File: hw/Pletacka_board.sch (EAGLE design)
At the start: 55 parts, among them U1 LM75BDP-NEW, U2 EL357N(A)(TA)-G, U3 EL357N(A)(TA)-G, U4 EL357N(A)(TA)-G, U5 EL357N(A)(TA)-G, U6 TPS54231D

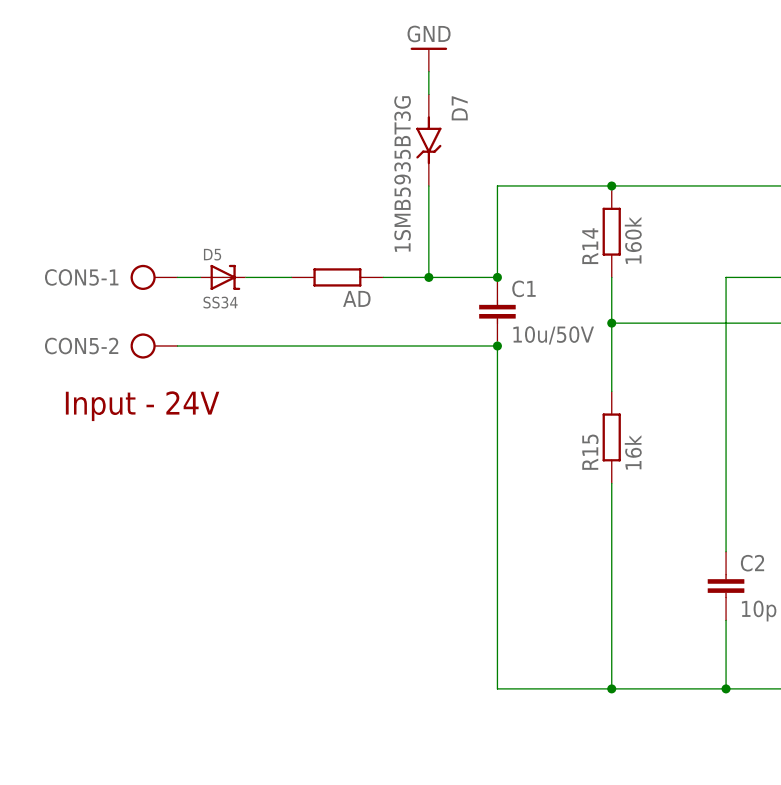
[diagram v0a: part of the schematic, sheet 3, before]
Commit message: Improve schema for step-down input
- improve readability of over-voltage protection in schema
- fix some minor issues (LCSC_IDs, ...)
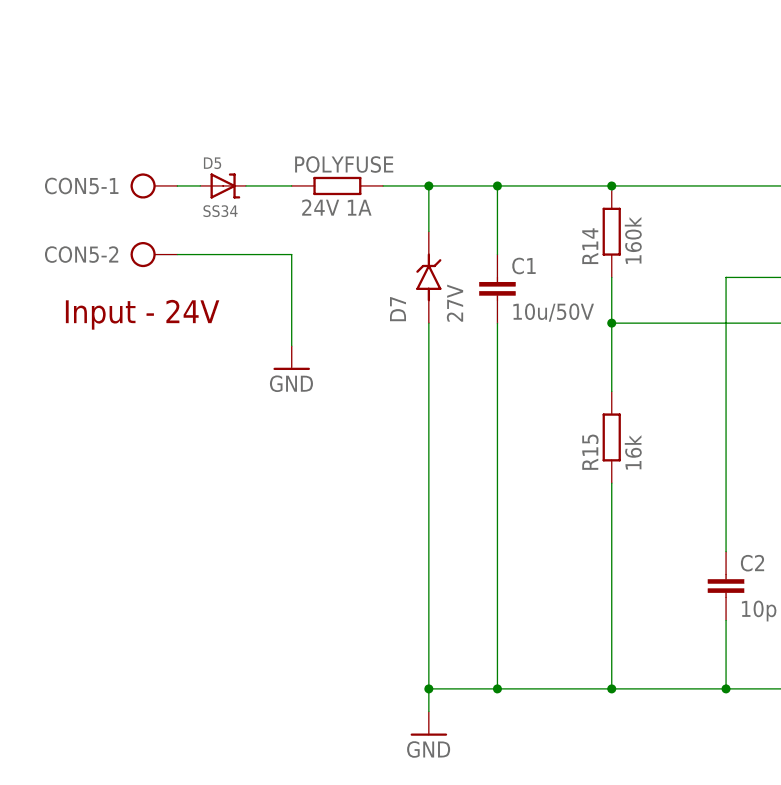
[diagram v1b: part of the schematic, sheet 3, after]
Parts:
- removed AD: (no value), rcl_upravena:R-EU_R1206
- added POLYFUSE: 24V 1A, rcl_upravena:R-EU_R1206
- D7: value 1SMB5935BT3G -> 27V; LCSC_ID (none) -> C49827
- U6: DESCRIPTION (none) -> 3.5 to 28V Input, 2A, 570kHz Step-Down Converter with Eco-m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
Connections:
- net N$4: now also POLYFUSE.2; no longer AD.2
- net VIN: now also POLYFUSE.1; no longer AD.1
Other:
- moved on the sheet: C1, CON5-1, CON5-2, D5, D7

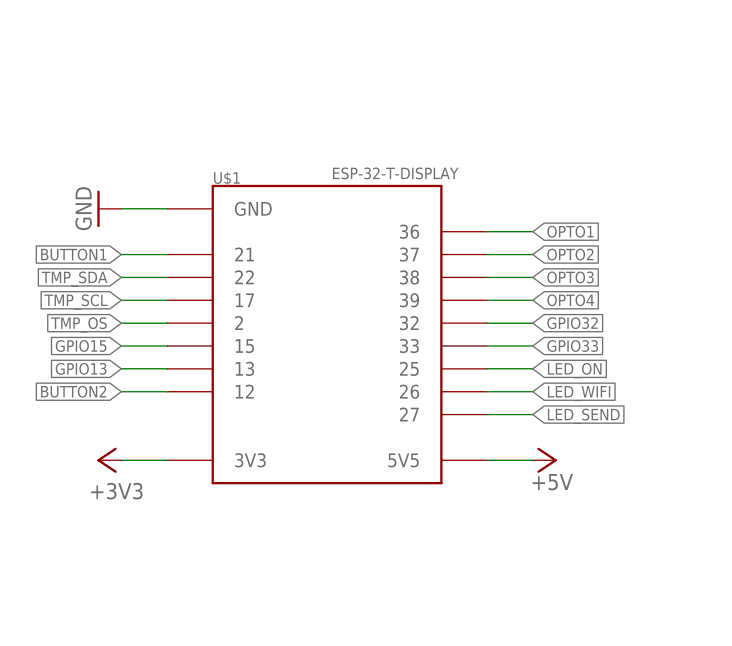
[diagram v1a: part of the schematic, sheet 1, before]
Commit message: Fix Beware of tombstoning (close #9)
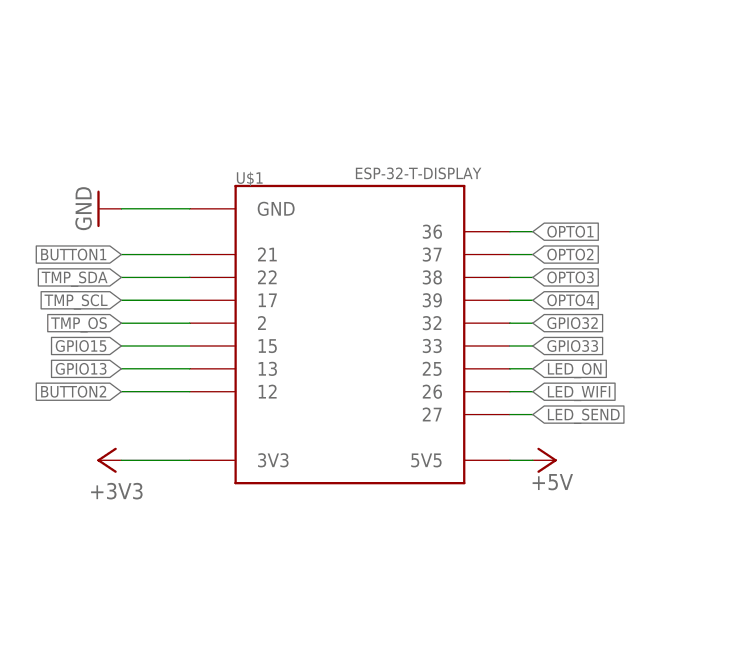
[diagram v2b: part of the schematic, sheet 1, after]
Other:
- moved on the sheet: U$1
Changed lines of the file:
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@@
 </spice>
 <attribute name="LCSC_ID" value="C22813"/>
-<attribute name="MFR_ID" value="nSMD050-24V
-"/>
+<attribute name="MFR_ID" value="nSMD050-24V "/>
 </part>
 <part name="GND14" library="supply1" library_urn="urn:adsk.eagle:library:371" deviceset="GND" device=""/>
@@
 <attribute name="SHEET" x="230.505" y="5.08" size="2.54" layer="94"/>
 </instance>
-<instance part="U$1" gate="G$1" x="66.04" y="96.52" smashed="yes">
-<attribute name="NAME" x="53.34" y="114.554" size="1.27" layer="95" font="vector" ratio="20"/>
-<attribute name="VALUE" x="66.548" y="115.062" size="1.27" layer="96" font="vector" ratio="20"/>
+<instance part="U$1" gate="G$1" x="68.58" y="96.52" smashed="yes">
+<attribute name="NAME" x="55.88" y="114.554" size="1.27" layer="95" font="vector" ratio="20"/>
+<attribute name="VALUE" x="69.088" y="115.062" size="1.27" layer="96" font="vector" ratio="20"/>
 </instance>
 <instance part="GND1" gate="1" x="40.64" y="111.76" smashed="yes" rot="R270">
@@
 <pinref part="GND1" gate="1" pin="GND"/>
 <pinref part="U$1" gate="G$1" pin="GND"/>
-<wire x1="43.18" y1="111.76" x2="48.26" y2="111.76" width="0.1524" layer="91"/>
+<wire x1="43.18" y1="111.76" x2="50.8" y2="111.76" width="0.1524" layer="91"/>
 </segment>
 <segment>
@@
 <pinref part="+3V1" gate="G$1" pin="+3V3"/>
 <pinref part="U$1" gate="G$1" pin="3V3"/>
-<wire x1="43.18" y1="83.82" x2="48.26" y2="83.82" width="0.1524" layer="91"/>
+<wire x1="43.18" y1="83.82" x2="50.8" y2="83.82" width="0.1524" layer="91"/>
 </segment>
 <segment>
@@
 <pinref part="U$1" gate="G$1" pin="5V5"/>
 <pinref part="P+1" gate="1" pin="+5V"/>
-<wire x1="83.82" y1="83.82" x2="88.9" y2="83.82" width="0.1524" layer="91"/>
+<wire x1="86.36" y1="83.82" x2="88.9" y2="83.82" width="0.1524" layer="91"/>
 </segment>
 <segment>
@@
 <segment>
 <pinref part="U$1" gate="G$1" pin="39"/>
-<wire x1="83.82" y1="101.6" x2="88.9" y2="101.6" width="0.1524" layer="91"/>
+<wire x1="86.36" y1="101.6" x2="88.9" y2="101.6" width="0.1524" layer="91"/>
 <label x="88.9" y="101.6" size="1.27" layer="95" xref="yes"/>
 </segment>
@@
 <segment>
 <pinref part="U$1" gate="G$1" pin="38"/>
-<wire x1="83.82" y1="104.14" x2="88.9" y2="104.14" width="0.1524" layer="91"/>
+<wire x1="86.36" y1="104.14" x2="88.9" y2="104.14" width="0.1524" layer="91"/>
 <label x="88.9" y="104.14" size="1.27" layer="95" xref="yes"/>
 </segment>
@@
 <segment>
 <pinref part="U$1" gate="G$1" pin="37"/>
-<wire x1="83.82" y1="106.68" x2="88.9" y2="106.68" width="0.1524" layer="91"/>
+<wire x1="86.36" y1="106.68" x2="88.9" y2="106.68" width="0.1524" layer="91"/>
 <label x="88.9" y="106.68" size="1.27" layer="95" xref="yes"/>
 </segment>
@@
 <segment>
 <pinref part="U$1" gate="G$1" pin="36"/>
-<wire x1="83.82" y1="109.22" x2="88.9" y2="109.22" width="0.1524" layer="91"/>
+<wire x1="86.36" y1="109.22" x2="88.9" y2="109.22" width="0.1524" layer="91"/>
 <label x="88.9" y="109.22" size="1.27" layer="95" xref="yes"/>
 </segment>
@@
 <segment>
 <pinref part="U$1" gate="G$1" pin="26"/>
-<wire x1="83.82" y1="91.44" x2="88.9" y2="91.44" width="0.1524" layer="91"/>
+<wire x1="86.36" y1="91.44" x2="88.9" y2="91.44" width="0.1524" layer="91"/>
 <label x="88.9" y="91.44" size="1.27" layer="95" xref="yes"/>
 </segment>
@@
 <segment>
 <pinref part="U$1" gate="G$1" pin="27"/>
-<wire x1="83.82" y1="88.9" x2="88.9" y2="88.9" width="0.1524" layer="91"/>
+<wire x1="86.36" y1="88.9" x2="88.9" y2="88.9" width="0.1524" layer="91"/>
 <label x="88.9" y="88.9" size="1.27" layer="95" xref="yes"/>
 </segment>
@@
 <segment>
 <pinref part="U$1" gate="G$1" pin="21"/>
-<wire x1="48.26" y1="106.68" x2="43.18" y2="106.68" width="0.1524" layer="91"/>
+<wire x1="50.8" y1="106.68" x2="43.18" y2="106.68" width="0.1524" layer="91"/>
 <label x="43.18" y="106.68" size="1.27" layer="95" rot="R180" xref="yes"/>
 </segment>
@@
 <segment>
 <pinref part="U$1" gate="G$1" pin="12"/>
-<wire x1="48.26" y1="91.44" x2="43.18" y2="91.44" width="0.1524" layer="91"/>
+<wire x1="50.8" y1="91.44" x2="43.18" y2="91.44" width="0.1524" layer="91"/>
 <label x="43.18" y="91.44" size="1.27" layer="95" rot="R180" xref="yes"/>
 </segment>
@@
 <segment>
 <pinref part="U$1" gate="G$1" pin="22"/>
-<wire x1="48.26" y1="104.14" x2="43.18" y2="104.14" width="0.1524" layer="91"/>
+<wire x1="50.8" y1="104.14" x2="43.18" y2="104.14" width="0.1524" layer="91"/>
 <label x="43.18" y="104.14" size="1.27" layer="95" rot="R180" xref="yes"/>
 </segment>
@@
 <segment>
 <pinref part="U$1" gate="G$1" pin="17"/>
-<wire x1="48.26" y1="101.6" x2="43.18" y2="101.6" width="0.1524" layer="91"/>
+<wire x1="50.8" y1="101.6" x2="43.18" y2="101.6" width="0.1524" layer="91"/>
 <label x="43.18" y="101.6" size="1.27" layer="95" rot="R180" xref="yes"/>
 </segment>
@@
 <segment>
 <pinref part="U$1" gate="G$1" pin="2"/>
-<wire x1="48.26" y1="99.06" x2="43.18" y2="99.06" width="0.1524" layer="91"/>
+<wire x1="50.8" y1="99.06" x2="43.18" y2="99.06" width="0.1524" layer="91"/>
 <label x="43.18" y="99.06" size="1.27" layer="95" rot="R180" xref="yes"/>
 </segment>
@@
 <segment>
 <pinref part="U$1" gate="G$1" pin="15"/>
-<wire x1="48.26" y1="96.52" x2="43.18" y2="96.52" width="0.1524" layer="91"/>
+<wire x1="50.8" y1="96.52" x2="43.18" y2="96.52" width="0.1524" layer="91"/>
 <label x="43.18" y="96.52" size="1.27" layer="95" rot="R180" xref="yes"/>
 </segment>
@@
 <segment>
 <pinref part="U$1" gate="G$1" pin="13"/>
-<wire x1="48.26" y1="93.98" x2="43.18" y2="93.98" width="0.1524" layer="91"/>
+<wire x1="50.8" y1="93.98" x2="43.18" y2="93.98" width="0.1524" layer="91"/>
 <label x="43.18" y="93.98" size="1.27" layer="95" rot="R180" xref="yes"/>
 </segment>
@@
 <segment>
 <pinref part="U$1" gate="G$1" pin="32"/>
-<wire x1="83.82" y1="99.06" x2="88.9" y2="99.06" width="0.1524" layer="91"/>
+<wire x1="86.36" y1="99.06" x2="88.9" y2="99.06" width="0.1524" layer="91"/>
 <label x="88.9" y="99.06" size="1.27" layer="95" xref="yes"/>
 </segment>
@@
 <segment>
 <pinref part="U$1" gate="G$1" pin="33"/>
-<wire x1="83.82" y1="96.52" x2="88.9" y2="96.52" width="0.1524" layer="91"/>
+<wire x1="86.36" y1="96.52" x2="88.9" y2="96.52" width="0.1524" layer="91"/>
 <label x="88.9" y="96.52" size="1.27" layer="95" xref="yes"/>
 </segment>
@@
 <segment>
 <pinref part="U$1" gate="G$1" pin="25"/>
-<wire x1="83.82" y1="93.98" x2="88.9" y2="93.98" width="0.1524" layer="91"/>
+<wire x1="86.36" y1="93.98" x2="88.9" y2="93.98" width="0.1524" layer="91"/>
 <label x="88.9" y="93.98" size="1.27" layer="95" xref="yes"/>
 </segment>

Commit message: Add pull-up resistors on I2C (close #14)
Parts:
- added R17, R18: 4k7, rcl_upravena:R-EU_R0603
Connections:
- net +3V3: now also R17.2, R18.2
- net TMP_SCL: now also R17.1
- net TMP_SDA: now also R18.1
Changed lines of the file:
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@@
 </part>
 <part name="GND15" library="supply1" library_urn="urn:adsk.eagle:library:371" deviceset="GND" device=""/>
+<part name="R17" library="rcl_upravena" deviceset="R-EU_" device="R0603" value="4k7">
+<attribute name="LCSC_ID" value="C23162"/>
+</part>
+<part name="R18" library="rcl_upravena" deviceset="R-EU_" device="R0603" value="4k7">
+<attribute name="LCSC_ID" value="C23162"/>
+</part>
+<part name="+3V8" library="supply1" library_urn="urn:adsk.eagle:library:371" deviceset="+3V3" device=""/>
+<part name="+3V9" library="supply1" library_urn="urn:adsk.eagle:library:371" deviceset="+3V3" device=""/>
 </parts>
 <sheets>
@@
 <attribute name="LCSC_ID" x="43.18" y="22.86" size="1.778" layer="96" rot="R90" display="off"/>
 </instance>
+<instance part="R17" gate="G$1" x="157.48" y="73.66" smashed="yes" rot="R90">
+<attribute name="NAME" x="155.9814" y="69.85" size="1.778" layer="95" rot="R90"/>
+<attribute name="VALUE" x="160.782" y="69.85" size="1.778" layer="96" rot="R90"/>
+<attribute name="LCSC_ID" x="157.48" y="73.66" size="1.778" layer="96" rot="R90" display="off"/>
+</instance>
+<instance part="R18" gate="G$1" x="220.98" y="81.28" smashed="yes" rot="R90">
+<attribute name="NAME" x="219.4814" y="77.47" size="1.778" layer="95" rot="R90"/>
+<attribute name="VALUE" x="224.282" y="77.47" size="1.778" layer="96" rot="R90"/>
+<attribute name="LCSC_ID" x="220.98" y="81.28" size="1.778" layer="96" rot="R90" display="off"/>
+</instance>
+<instance part="+3V8" gate="G$1" x="157.48" y="83.82" smashed="yes">
+<attribute name="VALUE" x="160.02" y="86.36" size="1.778" layer="96" rot="R180"/>
+</instance>
+<instance part="+3V9" gate="G$1" x="220.98" y="91.44" smashed="yes">
+<attribute name="VALUE" x="223.52" y="93.98" size="1.778" layer="96" rot="R180"/>
+</instance>
 </instances>
 <busses>
@@
 <pinref part="U1" gate="G$1" pin="SDA"/>
 <wire x1="215.9" y1="73.66" x2="220.98" y2="73.66" width="0.1524" layer="91"/>
-<label x="220.98" y="73.66" size="1.27" layer="95" xref="yes"/>
+<label x="228.6" y="73.66" size="1.27" layer="95" xref="yes"/>
+<pinref part="R18" gate="G$1" pin="1"/>
+<wire x1="220.98" y1="73.66" x2="228.6" y2="73.66" width="0.1524" layer="91"/>
+<wire x1="220.98" y1="76.2" x2="220.98" y2="73.66" width="0.1524" layer="91"/>
+<junction x="220.98" y="73.66"/>
 </segment>
 </net>
 <net name="TMP_SCL" class="0">
 <segment>
+<label x="147.32" y="68.58" size="1.27" layer="95" rot="R180" xref="yes"/>
+<pinref part="R17" gate="G$1" pin="1"/>
+<wire x1="157.48" y1="68.58" x2="147.32" y2="68.58" width="0.1524" layer="91"/>
 <pinref part="U1" gate="G$1" pin="SCL"/>
-<wire x1="180.34" y1="68.58" x2="175.26" y2="68.58" width="0.1524" layer="91"/>
-<label x="175.26" y="68.58" size="1.27" layer="95" rot="R180" xref="yes"/>
+<wire x1="157.48" y1="68.58" x2="180.34" y2="68.58" width="0.1524" layer="91"/>
+<junction x="157.48" y="68.58"/>
 </segment>
 </net>
@@
 <pinref part="R13" gate="G$1" pin="2"/>
 <pinref part="+3V6" gate="G$1" pin="+3V3"/>
+</segment>
+<segment>
+<pinref part="+3V8" gate="G$1" pin="+3V3"/>
+<pinref part="R17" gate="G$1" pin="2"/>
+<wire x1="157.48" y1="81.28" x2="157.48" y2="78.74" width="0.1524" layer="91"/>
+</segment>
+<segment>
+<pinref part="+3V9" gate="G$1" pin="+3V3"/>
+<pinref part="R18" gate="G$1" pin="2"/>
+<wire x1="220.98" y1="88.9" x2="220.98" y2="86.36" width="0.1524" layer="91"/>
 </segment>
 </net>
@@
 <segment>
 <pinref part="U1" gate="G$1" pin="OS"/>
-<wire x1="215.9" y1="71.12" x2="220.98" y2="71.12" width="0.1524" layer="91"/>
-<label x="220.98" y="71.12" size="1.27" layer="95" xref="yes"/>
-</segment>
-</net>
+<wire x1="215.9" y1="71.12" x2="228.6" y2="71.12" width="0.1524" layer="91"/>
+<label x="228.6" y="71.12" size="1.27" layer="95" xref="yes"/>
+</segment>
+</net>

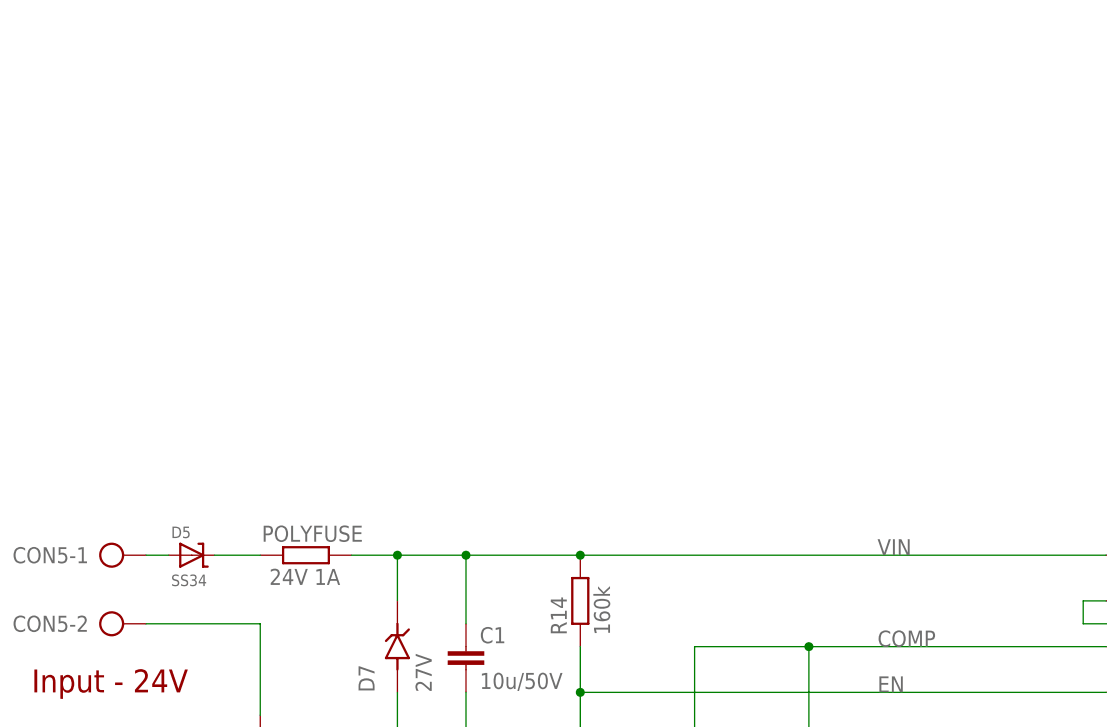
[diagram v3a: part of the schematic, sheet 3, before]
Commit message: Add input power voltage mesurement
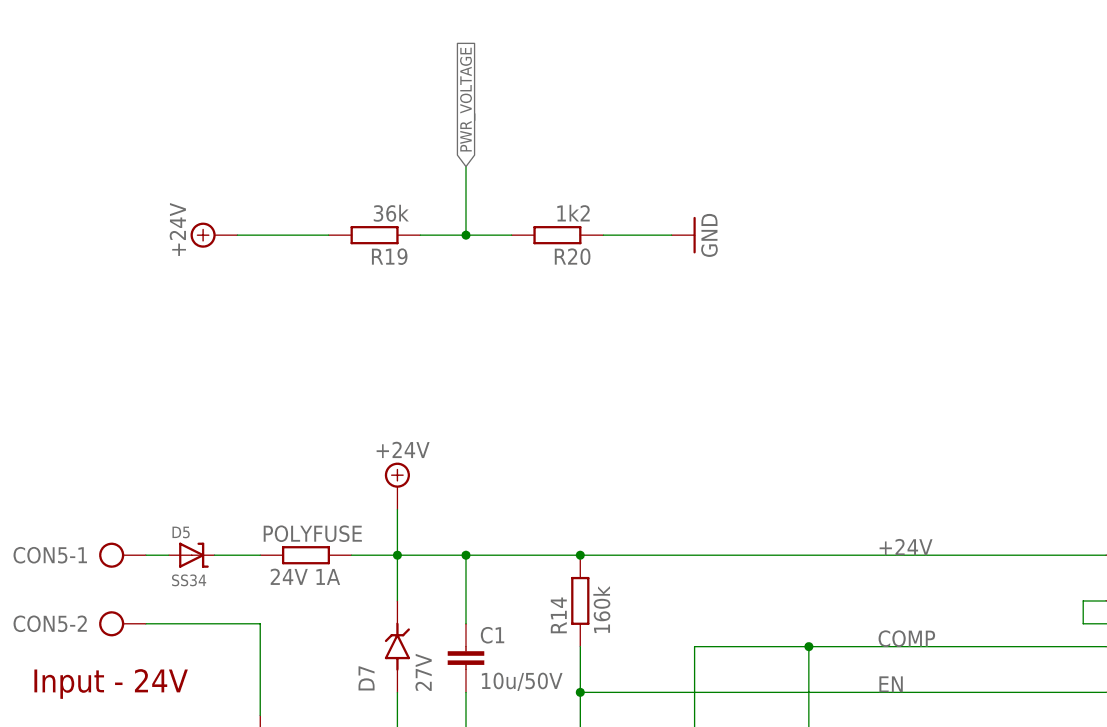
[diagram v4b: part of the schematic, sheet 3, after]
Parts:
- removed JP2, JP3: (no value), pinhead:PINHD-1X4
- added JP4, JP5: (no value), pinhead:PINHD-1X3
- added R19: 36k, rcl_upravena:R-EU_R0603
- added R20: 1k2, rcl_upravena:R-EU_R0603
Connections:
- removed net GPIO32: JP2.1, U$1.32
- removed net VIN: C1.1, D7.K, POLYFUSE.1, R14.2, U6.VIN
- new net +24V: C1.1, D7.K, POLYFUSE.1, R14.2, R19.2, U6.VIN
- new net PWR_VOLTAGE: R19.1, R20.2, U$1.32
- net GND: now also JP4.1, JP4.2, JP4.3, R20.1; no longer JP3.1, JP3.2, JP3.3, JP3.4
- net GPIO13: now also JP5.2; no longer JP2.3
- net GPIO15: now also JP5.3; no longer JP2.4
- net GPIO33: now also JP5.1; no longer JP2.2

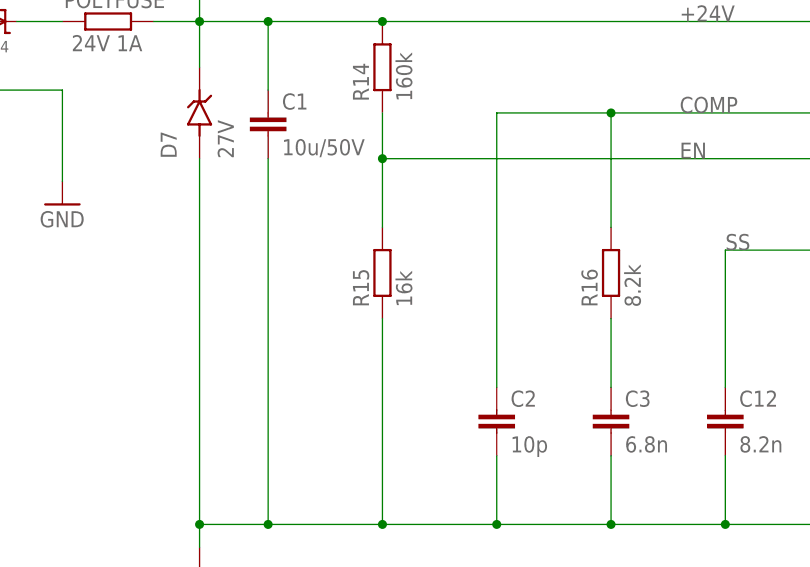
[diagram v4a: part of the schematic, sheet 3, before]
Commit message: Update resistor R15
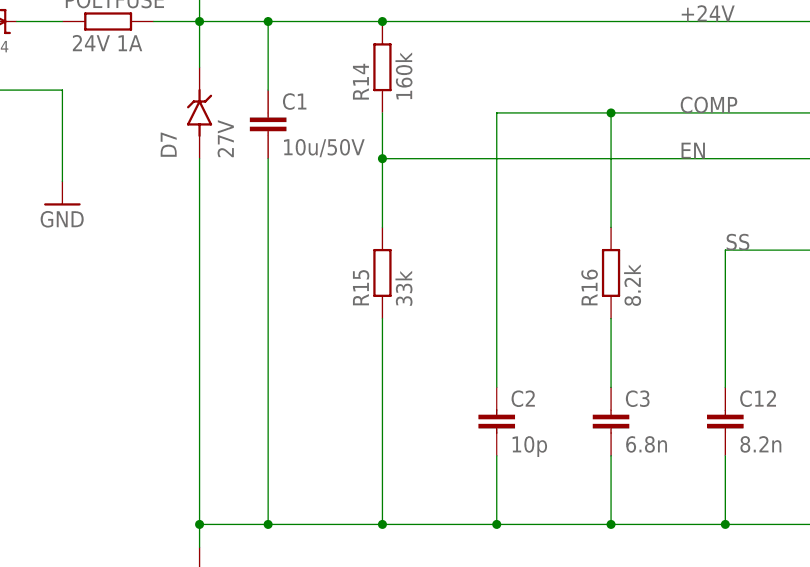
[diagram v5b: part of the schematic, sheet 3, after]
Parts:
- R15: value 16k -> 33k; LCSC_ID C22818 -> C4216
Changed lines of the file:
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@@
 <attribute name="LCSC_ID" value="C22813"/>
 </part>
-<part name="R15" library="rcl_upravena" deviceset="R-EU_" device="R0603" value="16k">
+<part name="R15" library="rcl_upravena" deviceset="R-EU_" device="R0603" value="33k">
 <spice>
 <pinmapping spiceprefix="R">
@@
 </pinmapping>
 </spice>
-<attribute name="LCSC_ID" value="C22818"/>
+<attribute name="LCSC_ID" value="C4216"/>
 </part>
 <part name="C2" library="rcl_upravena" deviceset="C-EU" device="C0603" value="10p">

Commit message: Update Polyfuse atribute
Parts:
- POLYFUSE: LCSC_ID C22813 -> C70076
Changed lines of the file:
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@@
 </pinmapping>
 </spice>
-<attribute name="LCSC_ID" value="C22813"/>
+<attribute name="LCSC_ID" value="C70076"/>
 <attribute name="MFR_ID" value="nSMD050-24V "/>
 </part>
